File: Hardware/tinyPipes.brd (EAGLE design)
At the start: 59 x 59 mm, 95 parts, among them Q1 CJ2302, Q5 S9013, Q6 S9013, Q7 S9013, U1 TD1410, U2 ICS_V54_SIM900, U3 ATMEGA168, U4 MAX4372, U5 SI4435POWER

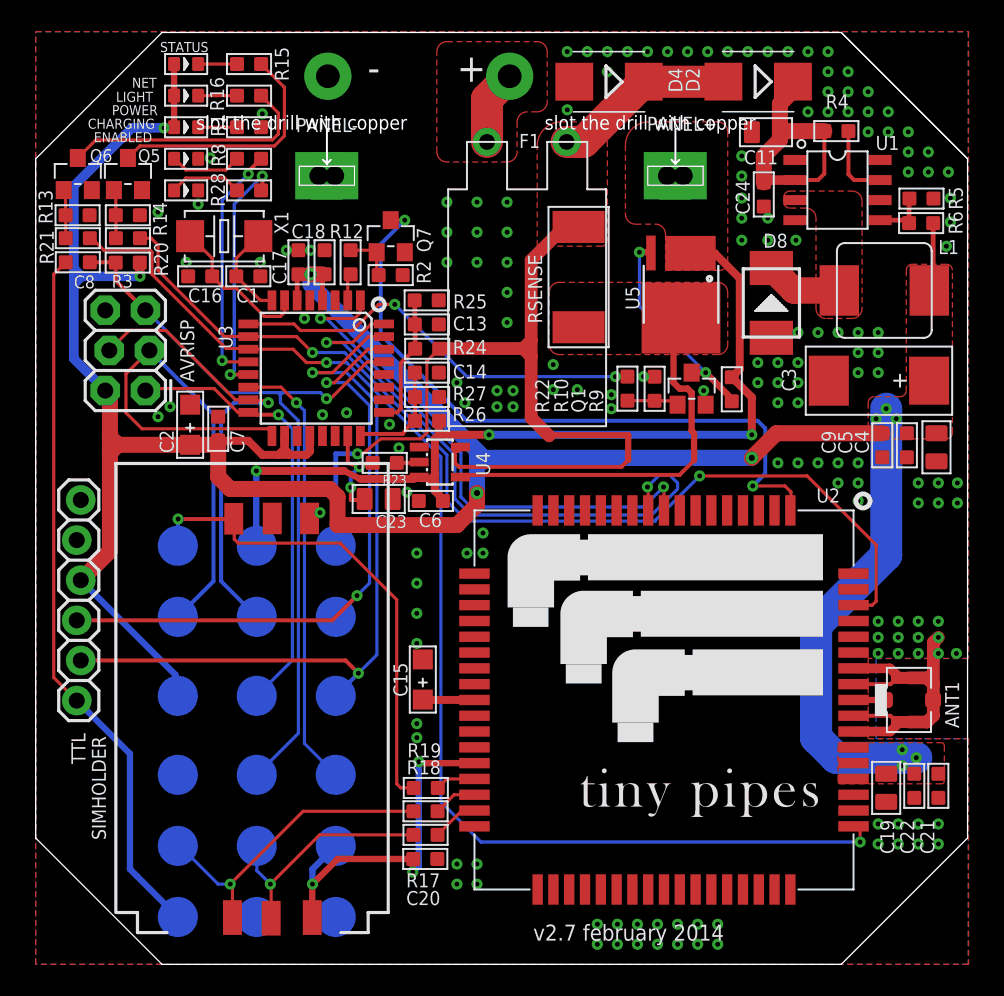
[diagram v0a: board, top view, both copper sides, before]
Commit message: ok, getspray is actually forwarding squirts up the server.  It's not a perfect sprinkler yet -- lots of hanging and restarting -- but it's really close
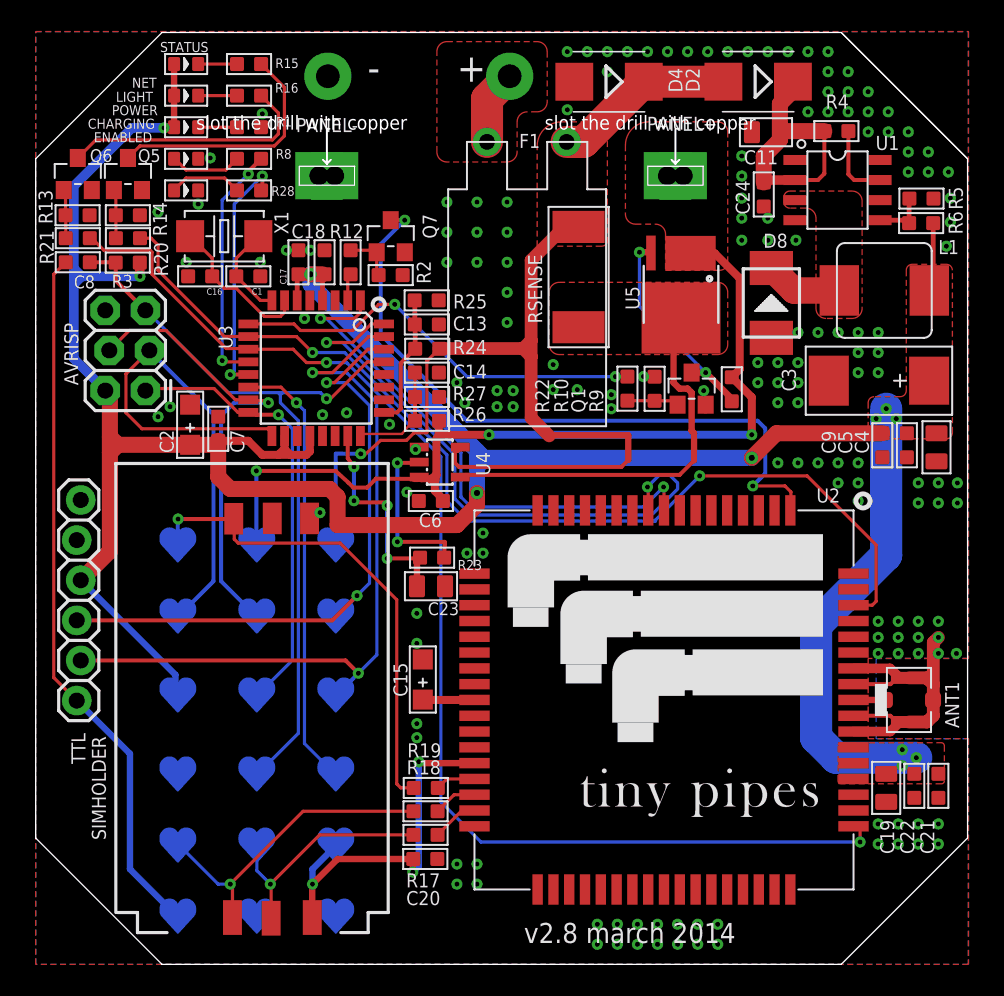
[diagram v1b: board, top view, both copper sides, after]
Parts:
- BATTERY, DTR, GND, GND1, GND11, GND2, LOAD_FET, MISO, MOSI, PANEL, RST, RST1, RX, SCK, SCK1, TX, VCC, VCC1: value PTR1B2,54 -> HEARTPAD; device testpad:B2,54 -> heart:HEART
- moved R23 6.71 mm to (25.1, 25.8)
- moved C23 6.44 mm to (25.0, 23.9)
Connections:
- net BATTERY: now also BATTERY.P$1; no longer BATTERY.TP
- net DTR: now also DTR.P$1; no longer DTR.TP
- net GND: now also GND.P$1, GND1.P$1, GND2.P$1; no longer GND.TP, GND1.TP, GND2.TP
- net LOAD_FET: now also LOAD_FET.P$1; no longer LOAD_FET.TP
- net MISO: now also MISO.P$1; no longer MISO.TP
- net MOSI: now also MOSI.P$1; no longer MOSI.TP
- net PANEL: now also PANEL.P$1; no longer PANEL.TP
- net RST: now also RST.P$1; no longer RST.TP
- net RX: now also RX.P$1; no longer RX.TP
- net SCK: now also SCK.P$1; no longer SCK.TP
- net SIM_CLK_DIRECT: now also VCC1.P$1; no longer VCC1.TP
- net SIM_DATA_DIRECT: now also GND11.P$1; no longer GND11.TP
- net SIM_RST_DIRECT: now also SCK1.P$1; no longer SCK1.TP
- net SIM_VDD: now also RST1.P$1; no longer RST1.TP
- net TX: now also TX.P$1; no longer TX.TP
- net VCC: now also VCC.P$1; no longer VCC.TP
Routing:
- net N$17: track 1.48 -> 10.4 mm, vias 0 -> 2
- net PANEL_CURRENT: track 6.59 -> 14.0 mm, vias 2 -> 4
- net PANEL: track 56.5 -> 57.0 mm
- net GND: vias 165 -> 163
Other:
- board text added: "v2.8 march 2014"
- board text removed: "v2.7 february 2014"

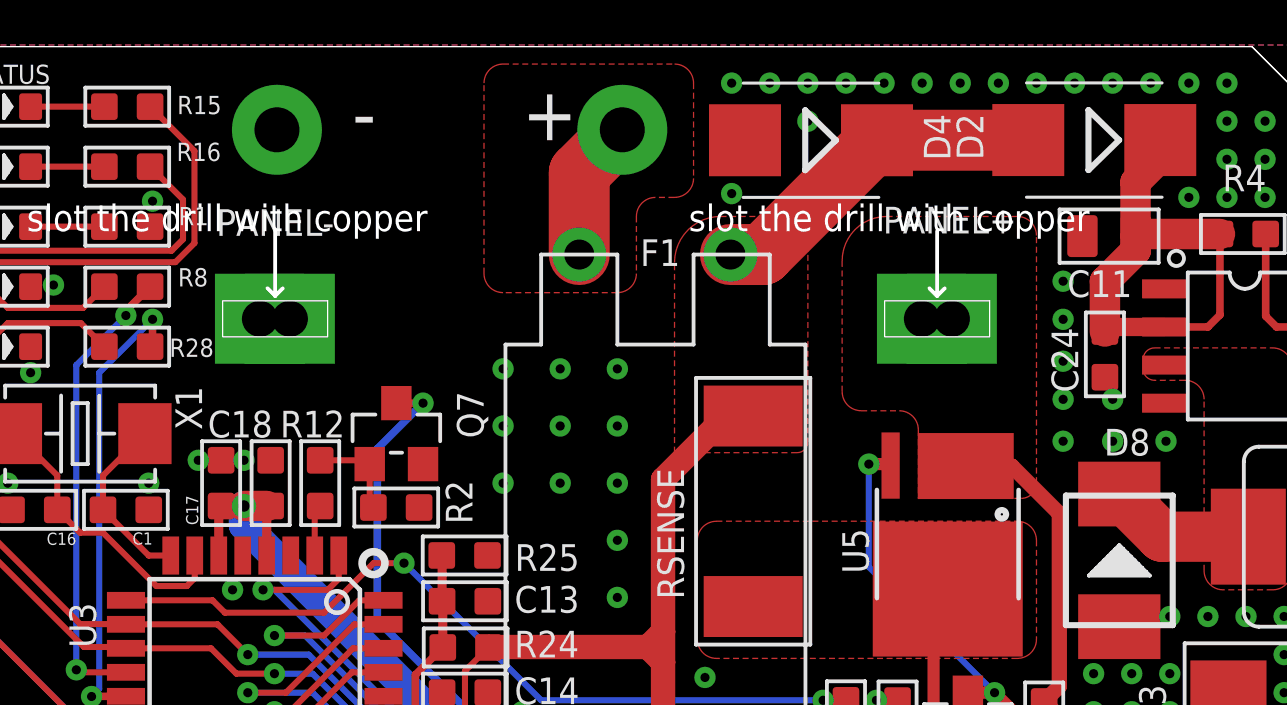
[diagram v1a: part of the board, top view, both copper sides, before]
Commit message: got rid of 'instantaneous' response and added more info to 'test' response
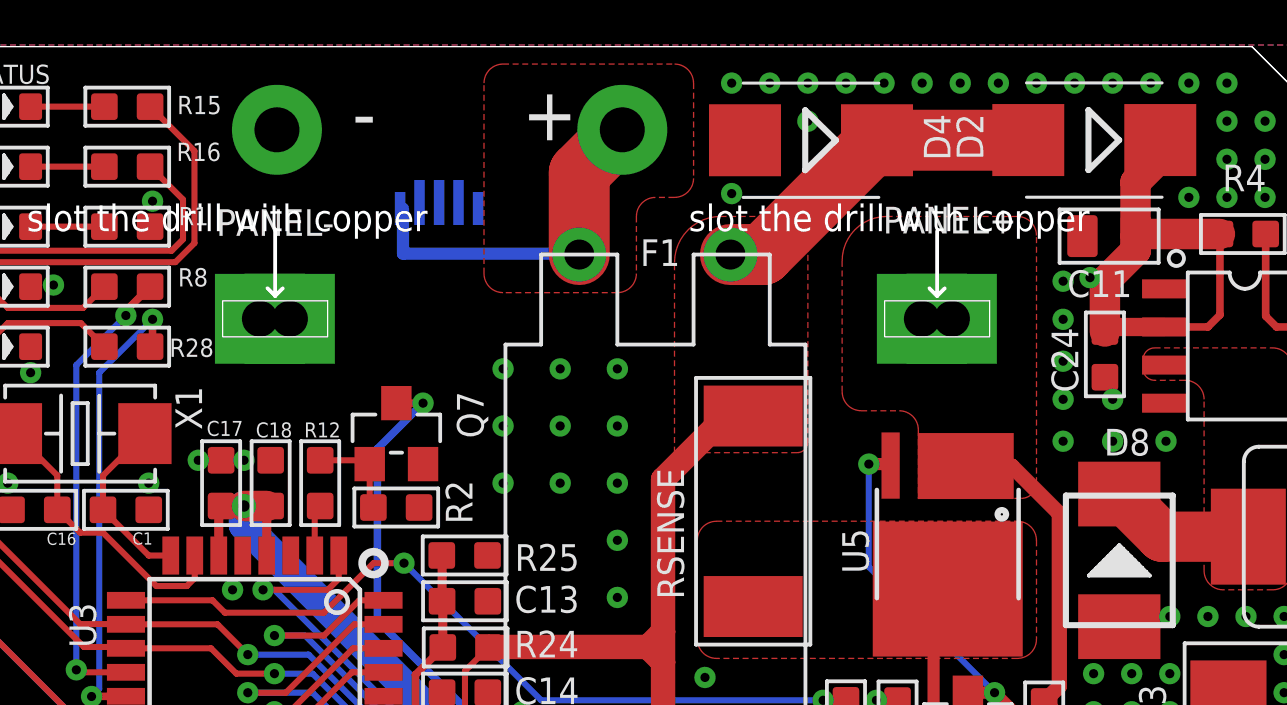
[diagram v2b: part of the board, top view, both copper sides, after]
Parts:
- added JP1: USB_MICROB_PLUG, SparkFun-Connectors:MICRO-B-RA-SMT
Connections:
- removed net RSENSE+: U4.4
- removed net RSENSE-: U4.5
- net BATT: now also JP1.1
- net BATTERY: now also U4.5
- net GND: now also JP1.5
- net PANEL_SWITCH: now also U4.4
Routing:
- net RSENSE+: track 25.3 -> 0.00 mm
- net PANEL_SWITCH: track 0.00 -> 25.3 mm
- net BATTERY: track 50.7 -> 69.8 mm
- net RSENSE-: track 19.1 -> 0.00 mm
- net BATT: track 4.75 -> 12.2 mm
- net VDD: track 16.7 -> 17.2 mm, vias 0 -> 1

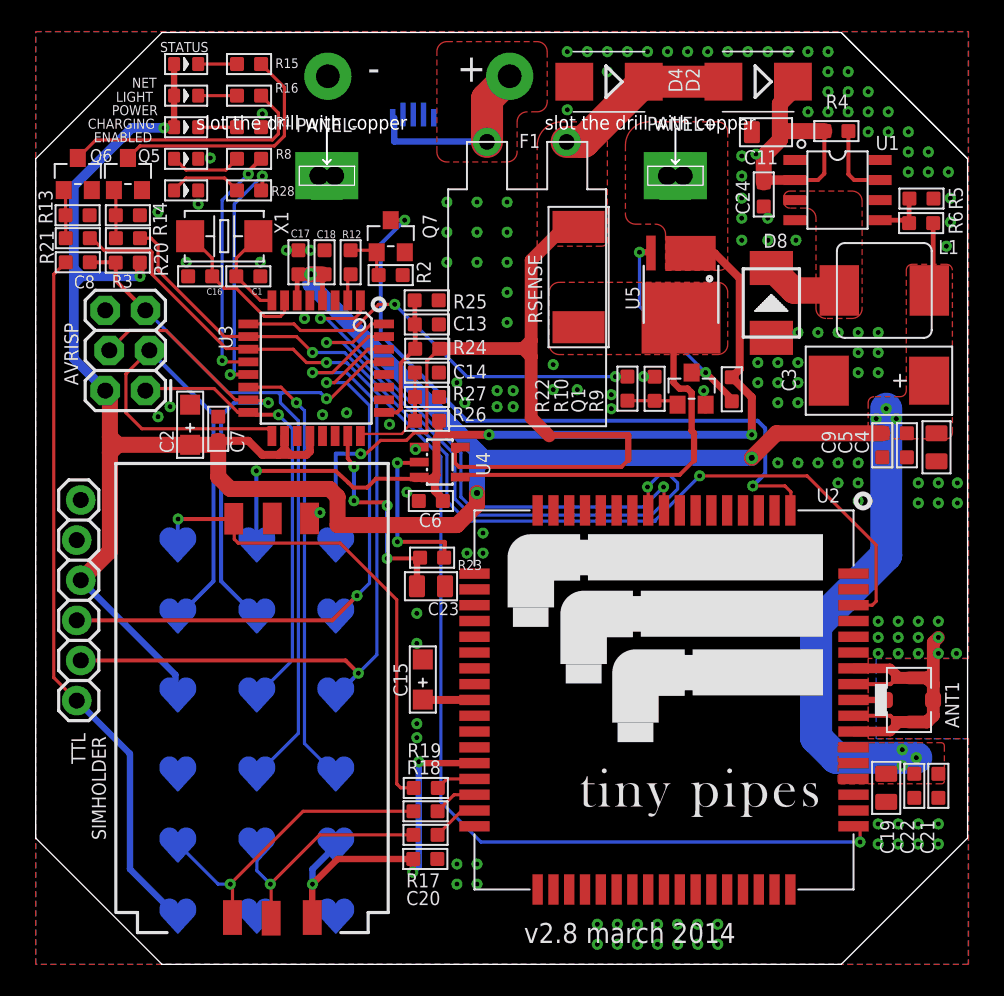
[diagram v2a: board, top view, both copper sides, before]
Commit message: finished design for tp v3.0, with pillowtalk, power the PCB from the panel, and a PCB antenna
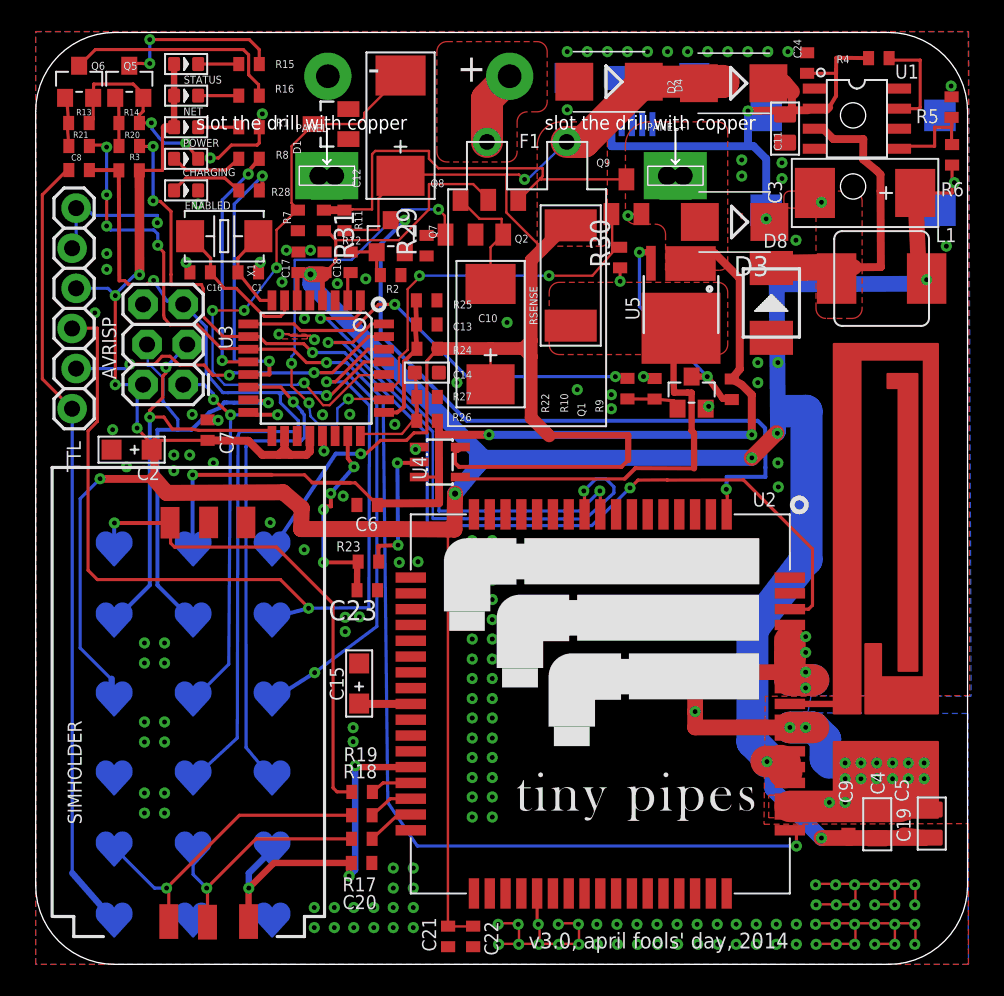
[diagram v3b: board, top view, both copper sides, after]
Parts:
- removed ANT1: (no value), Connector:4P-U-FL
- removed JP1: USB_MICROB_PLUG, SparkFun-Connectors:MICRO-B-RA-SMT
- added C10, C12: 470uF 6.3V, Discrete:AVX-D
- added D1: 5v, diode:SOT23
- added D3: SS54, diode:SMB
- added J1: Micro-USB connector, OPL Eagle Library:B-SMD-5P
- added Q2: BSS84, transistor-small-signal:SOT23
- added Q8, Q9: BSS123, transistor-small-signal:SOT23
- added R11: (no value), rcl:R0402
- added R29, R30, R31, R7: 10k, rcl:R0402
- added U$1: PCB_ANTENNA, tinyPipes:GSM_PCB_ANTENNA
- added U$4: BARREL_JACK, tinyPipes:BARREL_PLUG
- C1, C13, C16, C17, C18, C20, C21, C22, C24, C5, C6, C7, C8, C9: device Discrete:C0603 -> rcl:C0402
- C23: device Discrete:C0805 -> rcl:C0402
- R1, R10, R12, R13, R14, R15, R16, R17, R18, R19, R2, R20, R21, R22, R23, R24, R25, R26, R27, R28, R3, R4, R5, R6, R8, R9: device Discrete:R0603 -> rcl:R0402
- moved C21 32.5 mm to (26.1, 1.77)
- moved C22 29.5 mm to (27.7, 1.77)
- moved C4 24.2 mm to (53.3, 8.87), turned to 270 degrees
- moved C5 24.0 mm to (55.0, 8.83), turned to 270 degrees
- moved C9 24.0 mm to (51.5, 8.95), turned to 270 degrees
- moved TTL 18.5 mm to (2.31, 35.2)
- moved C3 11.9 mm to (52.5, 48.8)
- moved C24 8.76 mm to (48.8, 57.1), turned to 270 degrees
- moved R5 6.10 mm to (58.0, 54.3), turned to 90 degrees
- moved Q5 5.84 mm to (5.93, 55.9)
- moved Q6 5.84 mm to (2.75, 55.9)
- moved R13 5.84 mm to (2.74, 53.3)
- moved R14 5.84 mm to (5.92, 53.3)
- moved R20 5.84 mm to (5.93, 51.8)
- moved R21 5.84 mm to (2.75, 51.8)
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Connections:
- removed net ALT: U3.26
- removed net ALT2: U3.27
- removed net ALT3: U3.28
- new net HIGH_SIDE: Q9.1, R30.2, U3.27
- new net LOW_SIDE: Q8.1, R29.2, U3.26
- new net N$19: C10.-, Q2.3, Q8.3
- new net PFET_GATE: Q2.1, Q9.3, R11.1, R31.1
- new net PILLOWTALK_DATA_IN: C12.-, D1.3, R7.2, U3.28
- net BATT: no longer JP1.1
- net BATTERY: now also C10.+, C12.+, R11.2
- net GND: now also D1.1, J1.5, J1.E1, J1.E2, J1.P1, J1.P2, Q8.2, Q9.2, R29.1, R30.1, R7.1, U$1.GND, U$4.-@1, U$4.-@2; no longer ANT1.GND1, ANT1.GND2, ANT1.GND3, JP1.5
- net N$1: now also U$1.ANTENNA; no longer ANT1.D
- net PANEL: now also D3.A
- net VCC: now also Q2.2, R31.2
- net VDD: now also D3.C, J1.1, U$4.+@1, U$4.+@2
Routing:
- net GND: track 22.4 -> 119.8 mm, vias 163 -> 215
- net VCC: track 178.7 -> 253.7 mm, vias 11 -> 12
- net PILLOWTALK_DATA_IN: track 0.00 -> 39.4 mm, vias 0 -> 4
- net BATTERY: track 69.8 -> 100.2 mm, vias 1 -> 2
- net LOW_SIDE: track 0.00 -> 30.0 mm, vias 0 -> 4
- net PFET_GATE: track 0.00 -> 26.3 mm
- net HIGH_SIDE: track 0.00 -> 24.2 mm, vias 0 -> 2
- net RX: track 40.5 -> 59.1 mm
- net VDD: track 17.2 -> 34.1 mm, vias 1 -> 2
- net N$38: track 4.89 -> 19.8 mm
- net RST: track 49.9 -> 61.7 mm, vias 1 -> 2
- net N$19: track 0.00 -> 7.65 mm
- net BATT: track 12.2 -> 4.83 mm
- net PANEL: track 57.0 -> 64.1 mm
- net N$21: track 0.00 -> 6.95 mm
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- removed copper zone on layer 1, net VCC
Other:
- outline, holes or cut-outs redrawn
- board text added: "v3.0, april fools' day, 2014"
- board text removed: "LIGHT"
- board text removed: "v2.8 march 2014"

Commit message: tinyPipes v3.1
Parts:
- R11: value (none) -> 10k
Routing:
- net GND: vias 215 -> 211
